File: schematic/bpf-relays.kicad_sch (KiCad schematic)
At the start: 40 parts, among them U12 ULN2803A, U13 74HC238, U14 L78L33

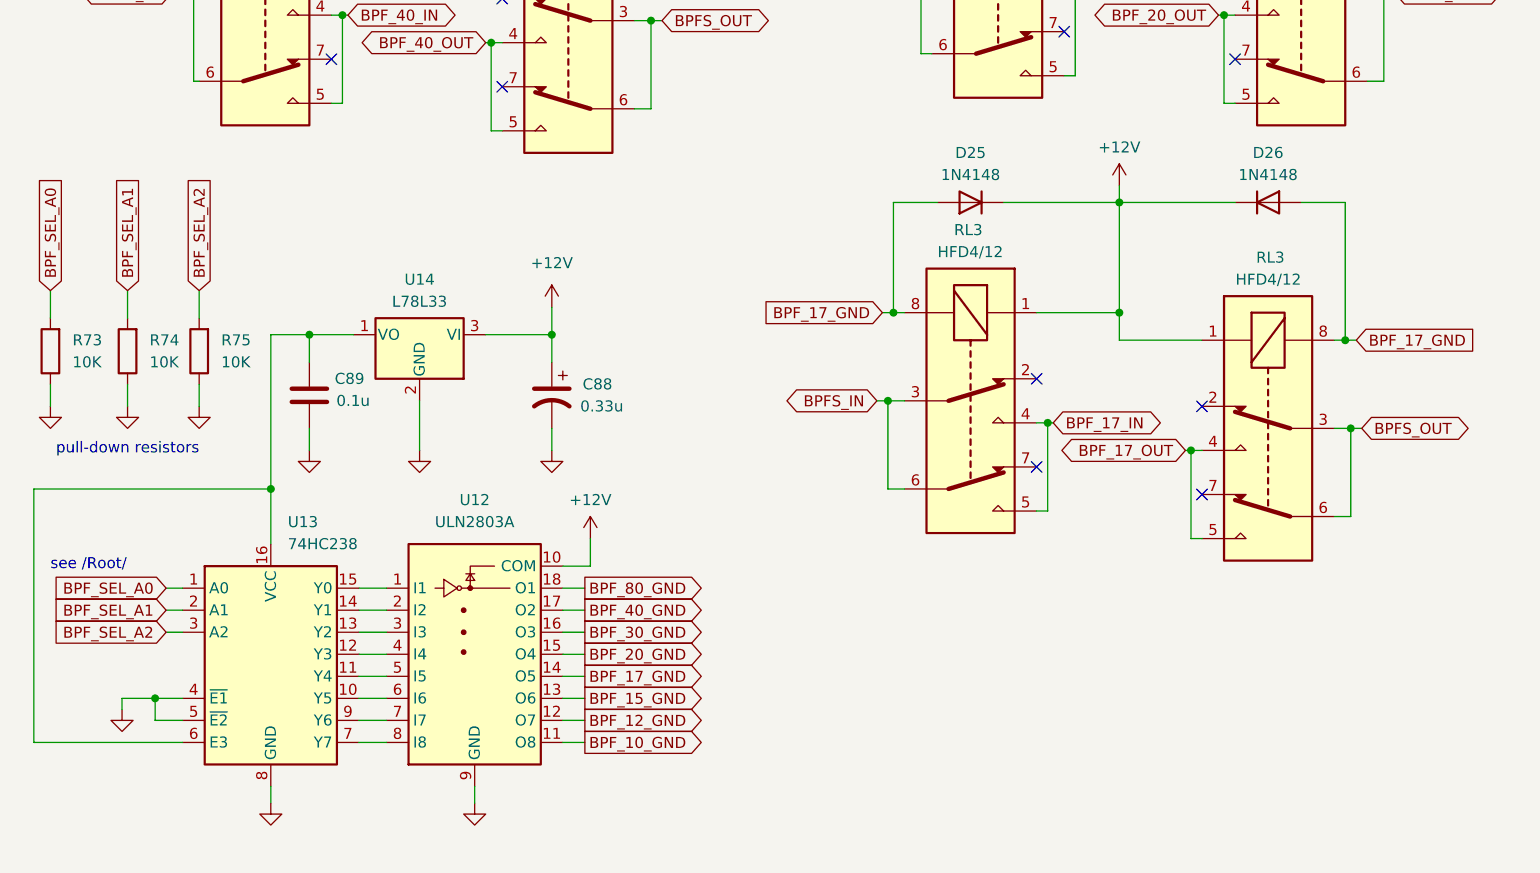
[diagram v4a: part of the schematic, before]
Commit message: Schematic: add a bit more 0.1u capacitors
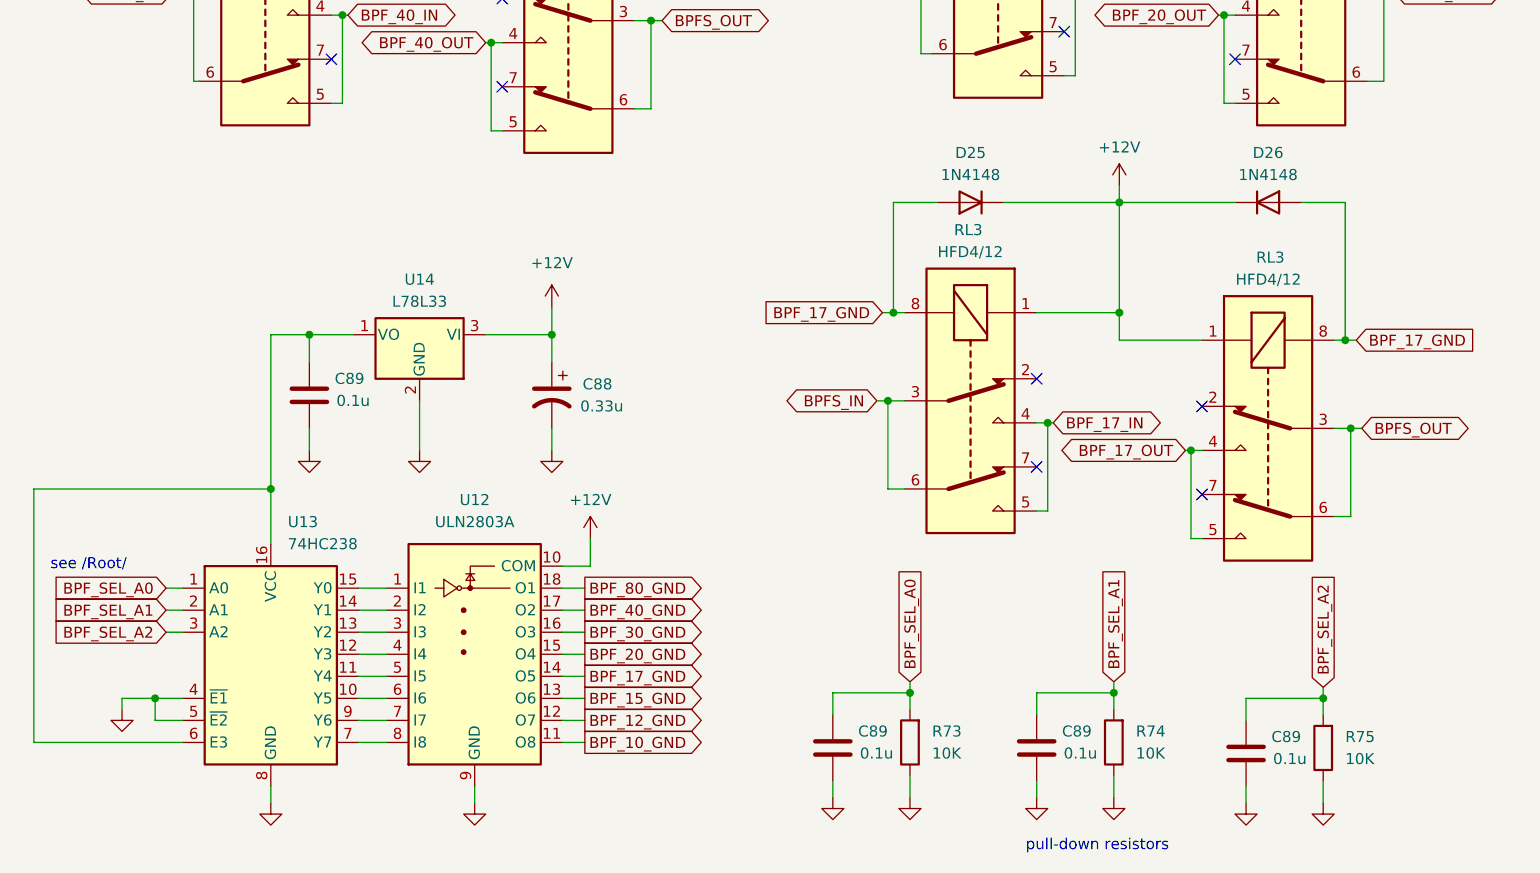
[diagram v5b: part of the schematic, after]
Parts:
- added C89 (x3): 0.1u, symbol Device:C
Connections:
- net BPF_SEL_A0: now also C89.2
- net BPF_SEL_A1: now also C89.2
- net BPF_SEL_A2: now also C89.2
- net GND: now also C89.1, C89.1, C89.1
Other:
- moved on the sheet: R73, R74, R75

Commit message: Minor changes
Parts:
- renumbered C89 to C208, C89 to C209, C89 to C210, RL3 to RL10, RL3 to RL11, RL3 to RL12, RL3 to RL13, RL3 to RL14, RL3 to RL15, RL3 to RL16, RL3 to RL17, RL3 to RL18, RL3 to RL19, RL3 to RL20, RL3 to RL21, RL3 to RL22, RL3 to RL23, RL3 to RL24, RL3 to RL9
